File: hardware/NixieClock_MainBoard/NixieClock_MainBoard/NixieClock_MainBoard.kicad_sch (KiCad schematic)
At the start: 6 parts, among them J1 Conn_01x14, J2 Conn_01x08, J3 Conn_01x08, J4 Conn_01x08, J5 Conn_01x08, U1 ESP32-WROOM-32E

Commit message: update: mainboard sheet
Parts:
- added J6: USB_C_Receptacle_USB2.0_16P, Connector_USB:USB_C_Receptacle_G-Switch_GT-USB-7010ASV, symbol Connector:USB_C_Receptacle_USB2.0_16P
- added U2: FT220XS, Package_QFP:LQFP-48_7x7mm_P0.5mm, symbol Interface_USB:FT220XS
- added U3: R-78C3.3-1.0, Converter_DCDC:Converter_DCDC_RECOM_R-78E-0.5_THT, symbol Regulator_Switching:R-78C3.3-1.0
- added U4: PCA9547D, Package_SO:SOIC-24W_7.5x15.4mm_P1.27mm, symbol Interface_Expansion:PCA9547D
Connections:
- new net: J6.A1 (GND), J6.A12 (GND), J6.B1 (GND), J6.B12 (GND)
- new net: J6.A4 (VBUS), J6.A9 (VBUS), J6.B4 (VBUS), J6.B9 (VBUS)
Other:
- note added: "Micro + OP (Für Effekte) BME 280 oder 680 breakout WS28... ein IO vorsehen. ein paar tasten durch Port-Expander - evtl. Radar-Taster.? Sleepmodus. --> Display ausschalten?"
- note added: "Wichtig pinout prüfen"
- note added: "Wichtig pinout prüfen. Welche Pins sollten nciht verwendet werden? Einige sind nur Output!!!"
- moved on the sheet: U1

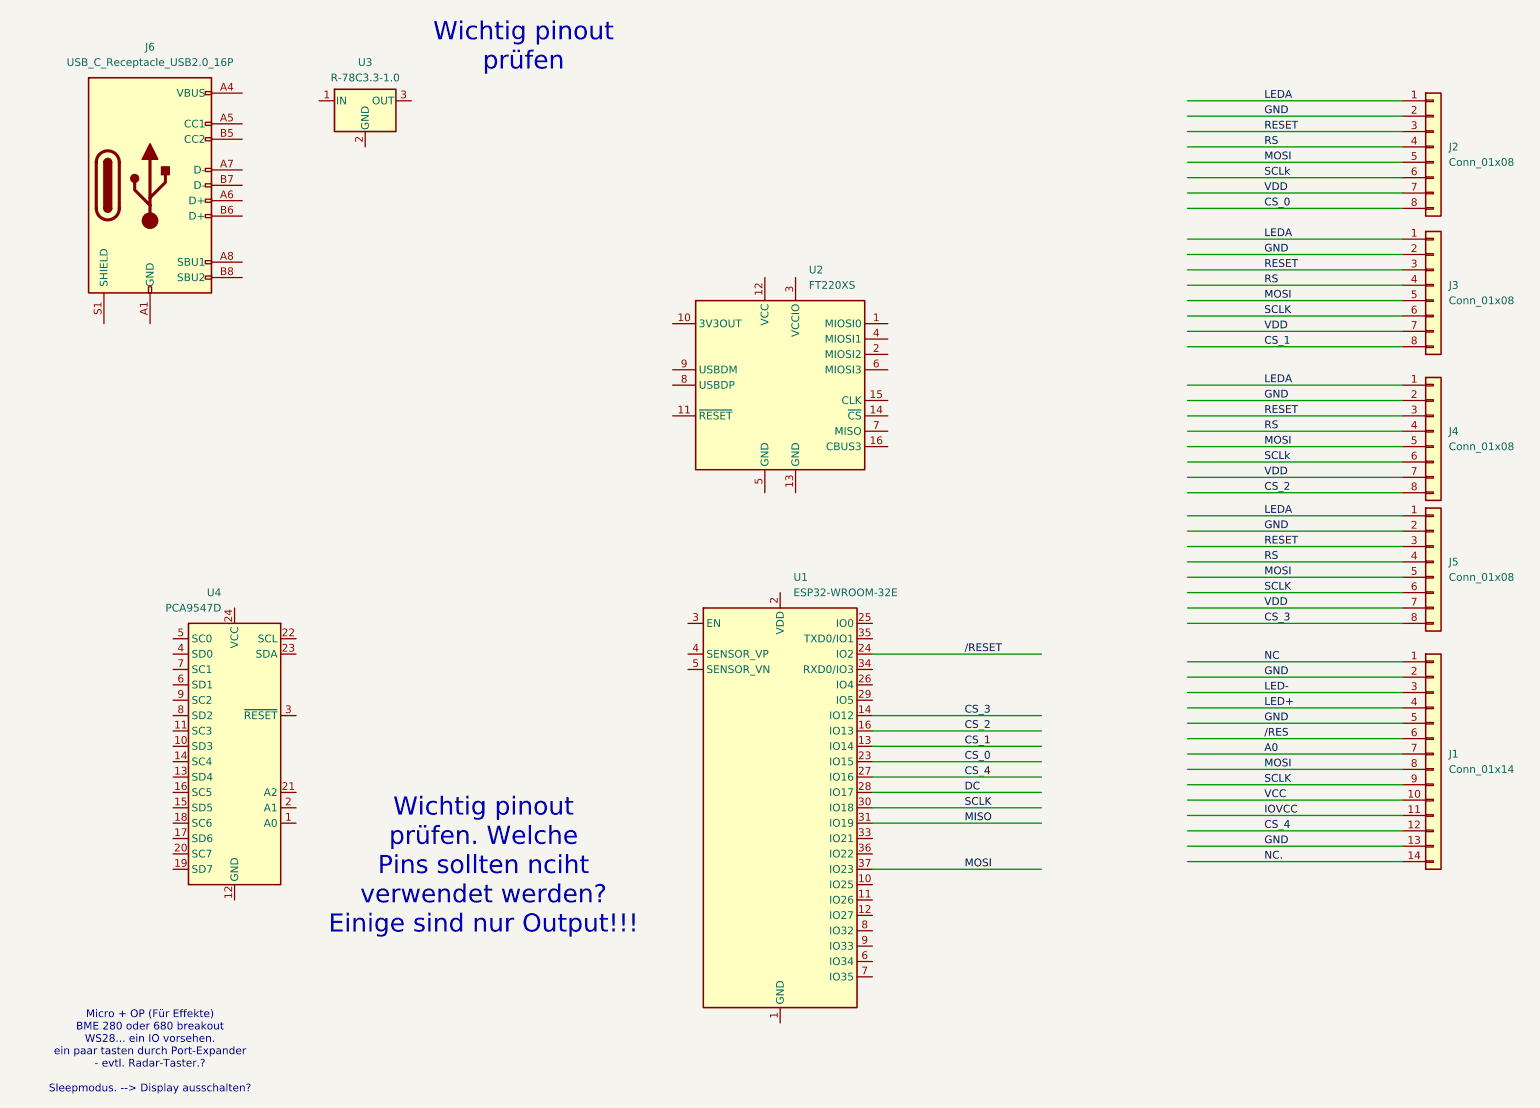
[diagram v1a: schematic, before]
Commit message: add mainboard schematic
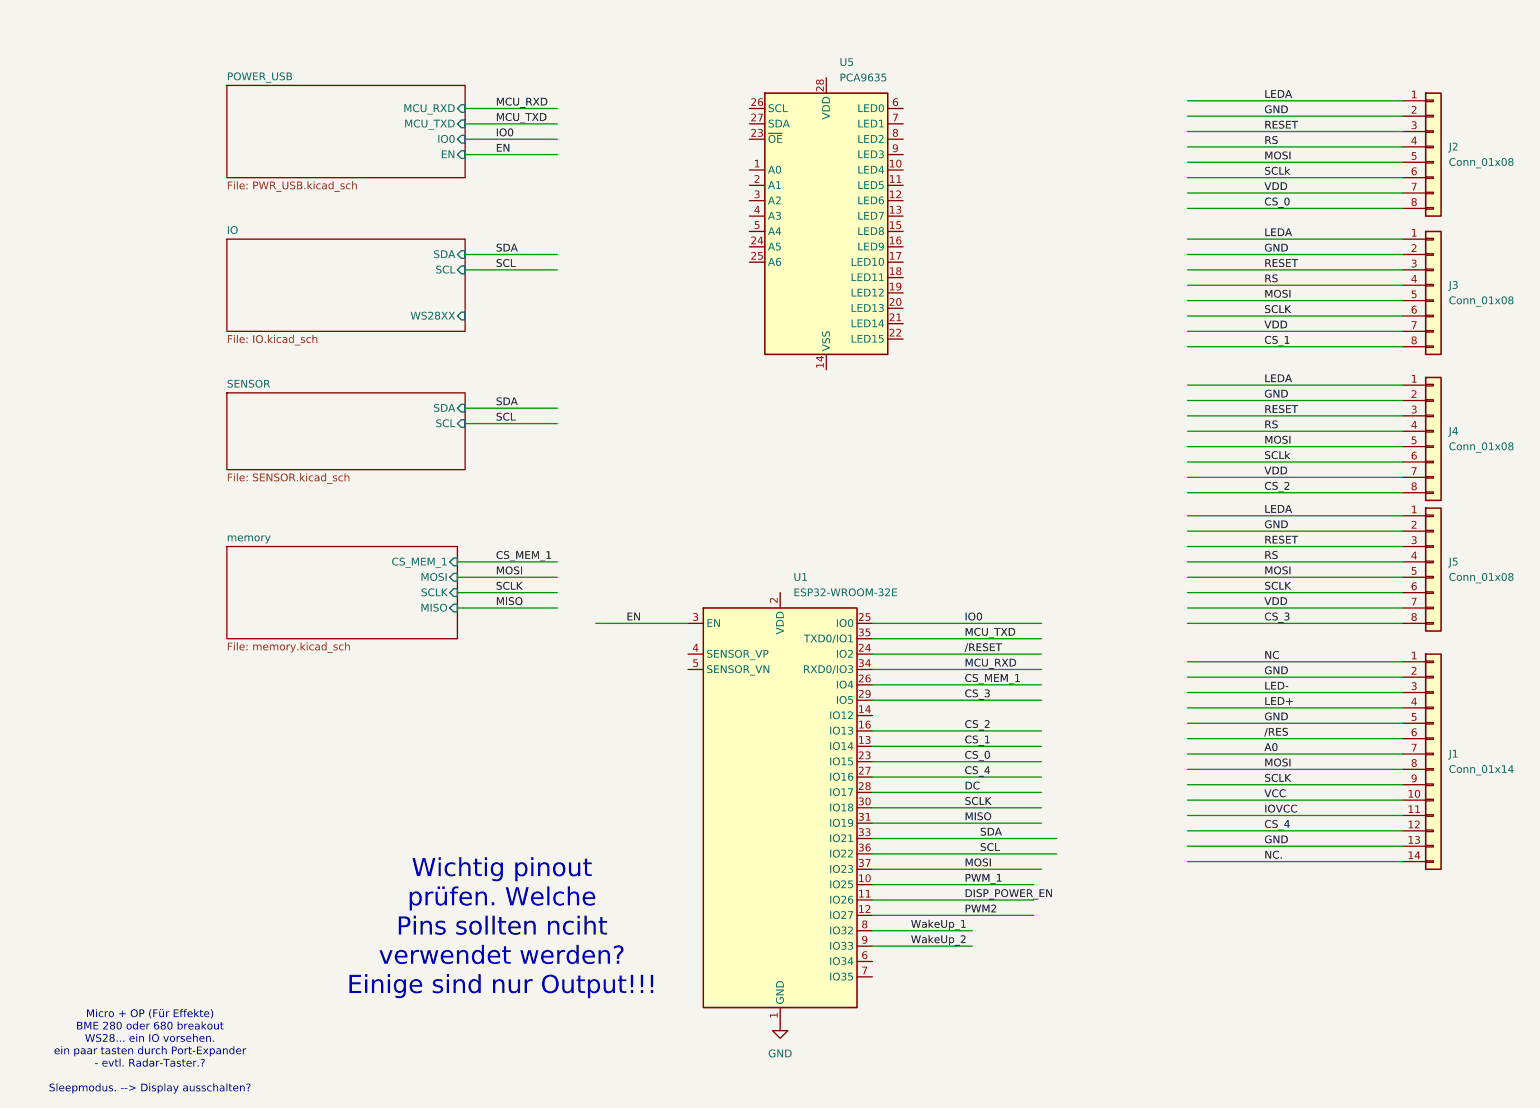
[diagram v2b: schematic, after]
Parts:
- removed J6: USB_C_Receptacle_USB2.0_16P, Connector_USB:USB_C_Receptacle_G-Switch_GT-USB-7010ASV, symbol Connector:USB_C_Receptacle_USB2.0_16P
- removed U2: FT220XS, Package_QFP:LQFP-48_7x7mm_P0.5mm, symbol Interface_USB:FT220XS
- removed U3: R-78C3.3-1.0, Converter_DCDC:Converter_DCDC_RECOM_R-78E-0.5_THT, symbol Regulator_Switching:R-78C3.3-1.0
- removed U4: PCA9547D, Package_SO:SOIC-24W_7.5x15.4mm_P1.27mm, symbol Interface_Expansion:PCA9547D
- added U5: PCA9635, Package_SO:TSSOP-28_4.4x9.7mm_P0.65mm, symbol Driver_LED:PCA9635
- J1: footprint Connector_PinHeader_1.27mm:PinHeader_1x14_P1.27mm_Vertical -> Connector_PinSocket_1.27mm:PinSocket_1x14_P1.27mm_Vertical
- J2, J3, J4, J5: footprint Connector_PinHeader_1.27mm:PinHeader_1x08_P1.27mm_Vertical -> Connector_PinSocket_1.27mm:PinSocket_1x08_P1.27mm_Vertical
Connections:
- net CS_3: now also U1.29 (IO5); no longer U1.14 (IO12)
- net GND: now also U1.1 (GND), U1.15 (GND), U1.38 (GND), U1.39 (GND)
- net PWM_1: now reaches U1.10 (IO25)
- net DISP_POWER_EN: now reaches U1.11 (IO26)
- net PWM2: now reaches U1.12 (IO27)
- net IO0: now reaches U1.25 (IO0)
- net CS_MEM_1: now reaches U1.26 (IO4)
- net EN: now reaches U1.3 (EN)
- net SDA: now reaches U1.33 (IO21)
- net MCU_RXD: now reaches U1.34 (RXD0/IO3)
- net MCU_TXD: now reaches U1.35 (TXD0/IO1)
- net SCL: now reaches U1.36 (IO22)
- net WakeUp_1: now reaches U1.8 (IO32)
- net WakeUp_2: now reaches U1.9 (IO33)
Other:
- added sheet IO (IO.kicad_sch)
- added sheet POWER_USB (PWR_USB.kicad_sch)
- added sheet SENSOR (SENSOR.kicad_sch)
- added sheet memory (memory.kicad_sch)
- note removed: "Wichtig pinout prüfen"

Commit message: layout mainboard
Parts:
- removed U1: ESP32-WROOM-32E, RF_Module:ESP32-WROOM-32D, symbol RF_Module:ESP32-WROOM-32E
- removed U5: PCA9635, Package_SO:TSSOP-28_4.4x9.7mm_P0.65mm, symbol Driver_LED:PCA9635
- added R13, R14, R15, R16, R17, R18, R19, R20, R21, R7, R8: 10k, Resistor_SMD:R_0603_1608Metric, symbol Device:R
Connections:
- net LED- is gone; now on net GND: J1.3 (Pin_3)
- net A0: now also R20.1; no longer J1.7 (Pin_7)
- net IOVCC: now also R21.2
- net RS: now also R13.1, R15.1, R17.1, R8.1; no longer J2.4 (Pin_4), J3.4 (Pin_4), J4.4 (Pin_4), J5.4 (Pin_4)
- net VCC: now also R21.1
- net LED+ renamed LED_PWM_4
- removed net LEDA: J2.1 (Pin_1), J3.1 (Pin_1), J4.1 (Pin_1), J5.1 (Pin_1)
- net NC: no longer names the net of J1.1 (Pin_1)
- net NC.: no longer names the net of J1.14 (Pin_14)
- removed net RESET: J2.3 (Pin_3), J3.3 (Pin_3), J4.3 (Pin_3), J5.3 (Pin_3)
- net /RES: no longer names the net of J1.6 (Pin_6)
- net /RES: now also R19.2
- new net: J4.4 (Pin_4), R15.2
- new net: J5.4 (Pin_4), R17.2
- new net: J2.3 (Pin_3), R7.2
- new net: J2.4 (Pin_4), R8.2
- new net: J3.3 (Pin_3), R14.2
- new net: J3.4 (Pin_4), R13.2
- new net: J4.3 (Pin_3), R16.2
- new net: J5.3 (Pin_3), R18.2
- new net: J1.7 (Pin_7), R20.2
- new net LED_PWM_0: J2.1 (Pin_1)
- new net LED_PWM_1: J3.1 (Pin_1)
- new net LED_PWM_2: J4.1 (Pin_1)
- new net LED_PWM_3: J5.1 (Pin_1)
- new net ~{RESET}: R14.1, R16.1, R18.1, R19.1, R7.1
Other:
- added sheet pwm (pwm.kicad_sch)
- added sheet uC (uC.kicad_sch)
- sheet IO ports: added ~{INT_IO}; removed none
- note removed: "Wichtig pinout prüfen. Welche Pins sollten nciht verwendet werden? Einige sind nur Output!!!"

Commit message: update mainboard
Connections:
- net SCLk is gone; now on net SCLK: J2.6 (Pin_6), J4.6 (Pin_6)
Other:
- sheet uC ports: added WS28XX; removed none
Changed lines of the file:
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@@
 	(wire
 		(pts
+			(xy 124.46 127) (xy 139.7 127)
+		)
+		(stroke
+			(width 0)
+			(type default)
+		)
+	)
+	(wire
+		(pts
 			(xy 124.46 93.98) (xy 139.7 93.98)
 		)
@@
 		)
 	)
-	(label "SCLk"
+	(label "SCLK"
 		(at 222.25 40.64 0)
 		(fields_autoplaced yes)
@@
 		)
 	)
+	(label "WS28XX"
+		(at 129.54 127 0)
+		(fields_autoplaced yes)
+		(effects
+			(font
+				(size 1.27 1.27)
+			)
+			(justify left bottom)
+		)
+	)
 	(label "VDD"
 		(at 222.25 111.76 0)
@@
 		)
 	)
-	(label "SCLk"
+	(label "SCLK"
 		(at 222.25 87.63 0)
 		(fields_autoplaced yes)
@@
 			)
 		)
+		(pin "WS28XX" output
+			(at 139.7 127 180)
+			(effects
+				(font
+					(size 1.27 1.27)
+				)
+				(justify left)
+			)
+		)
